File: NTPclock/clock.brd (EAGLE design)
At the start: 100 x 100 mm, 21 parts, among them IC1 MAX7219CNG

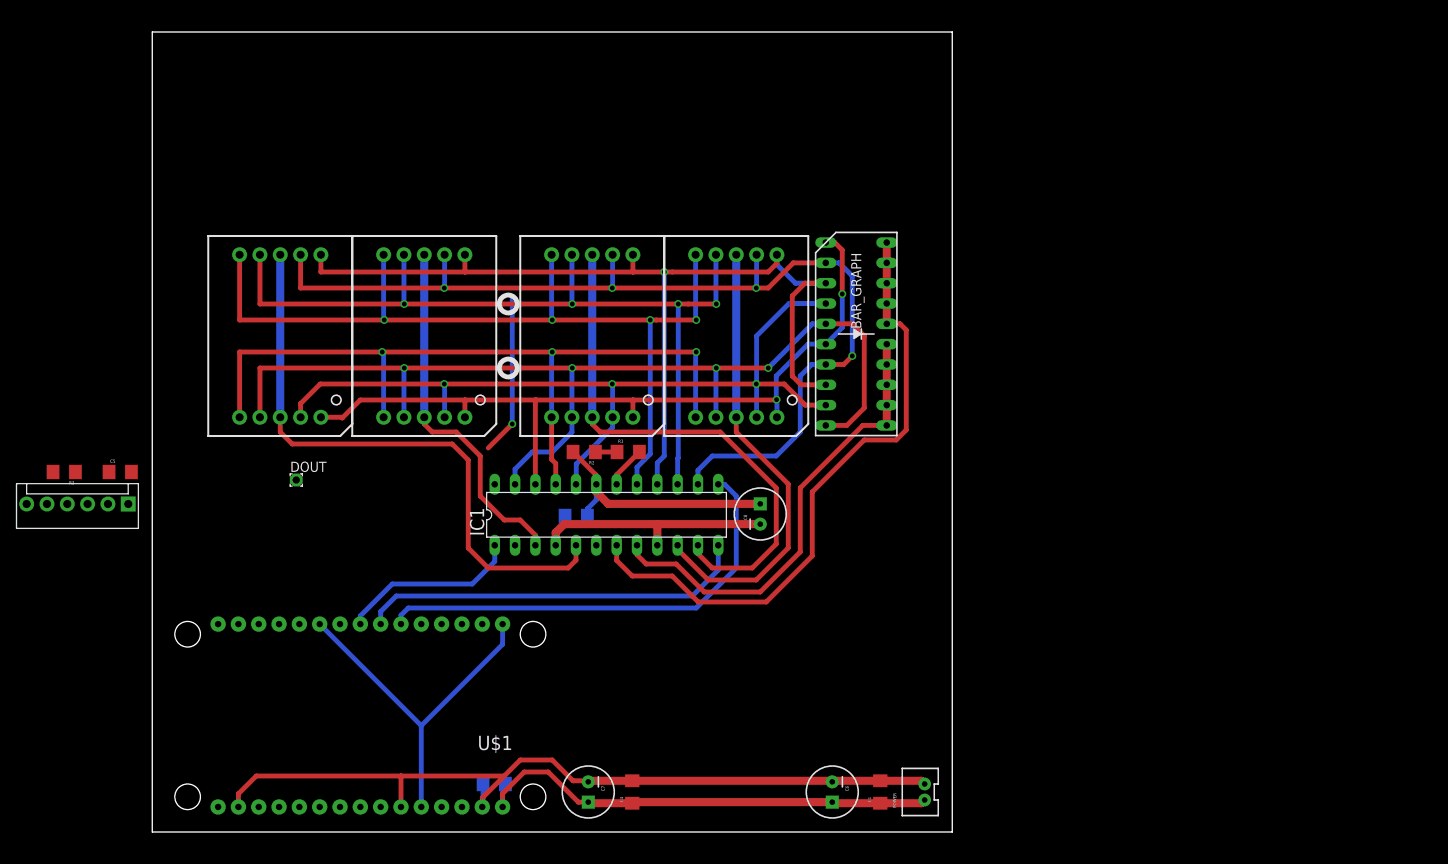
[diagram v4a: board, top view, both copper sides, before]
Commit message: Add Ground pour(s)
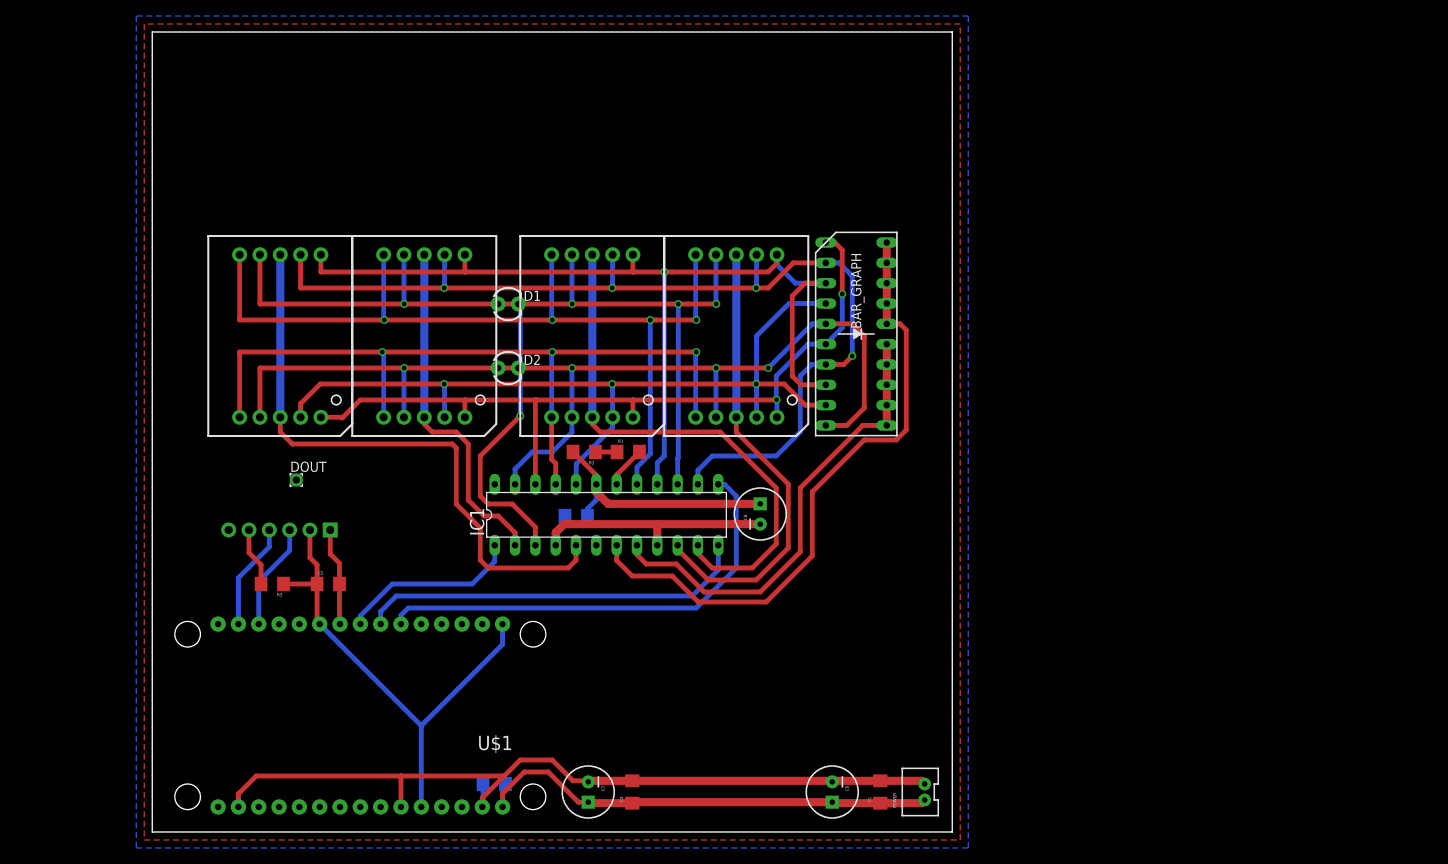
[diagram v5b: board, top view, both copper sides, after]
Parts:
- added D1, D2: (no value), SparkFun-LED:LED3MM
- moved C5 29.5 mm to (22.0, 31.0)
- moved R3 29.5 mm to (15.0, 31.0)
- moved J1 25.5 mm to (22.2, 37.8), flipped to the bottom, turned to 0 degrees
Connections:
- net DIGIT0: now also DIG_1.3, DIG_1.8
- net DIGIT4: now also D1.K, D2.K; no longer DIG_1.3, DIG_1.8
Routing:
- net DIGIT0: track 20.2 -> 43.8 mm, vias 1 -> 0
- net 3.3V: track 45.0 -> 61.5 mm
- net SDA: track 0.00 -> 13.4 mm
- net SCL: track 0.00 -> 13.4 mm
- net GND: track 136.9 -> 149.2 mm
- net DIGIT4: track 45.0 -> 37.1 mm, vias 0 -> 1
- net SQL: track 0.00 -> 7.38 mm
- added copper zone on layer 1, net GND
- added copper zone on layer 16, net GND

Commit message: added buzzer, finished routing ground plane
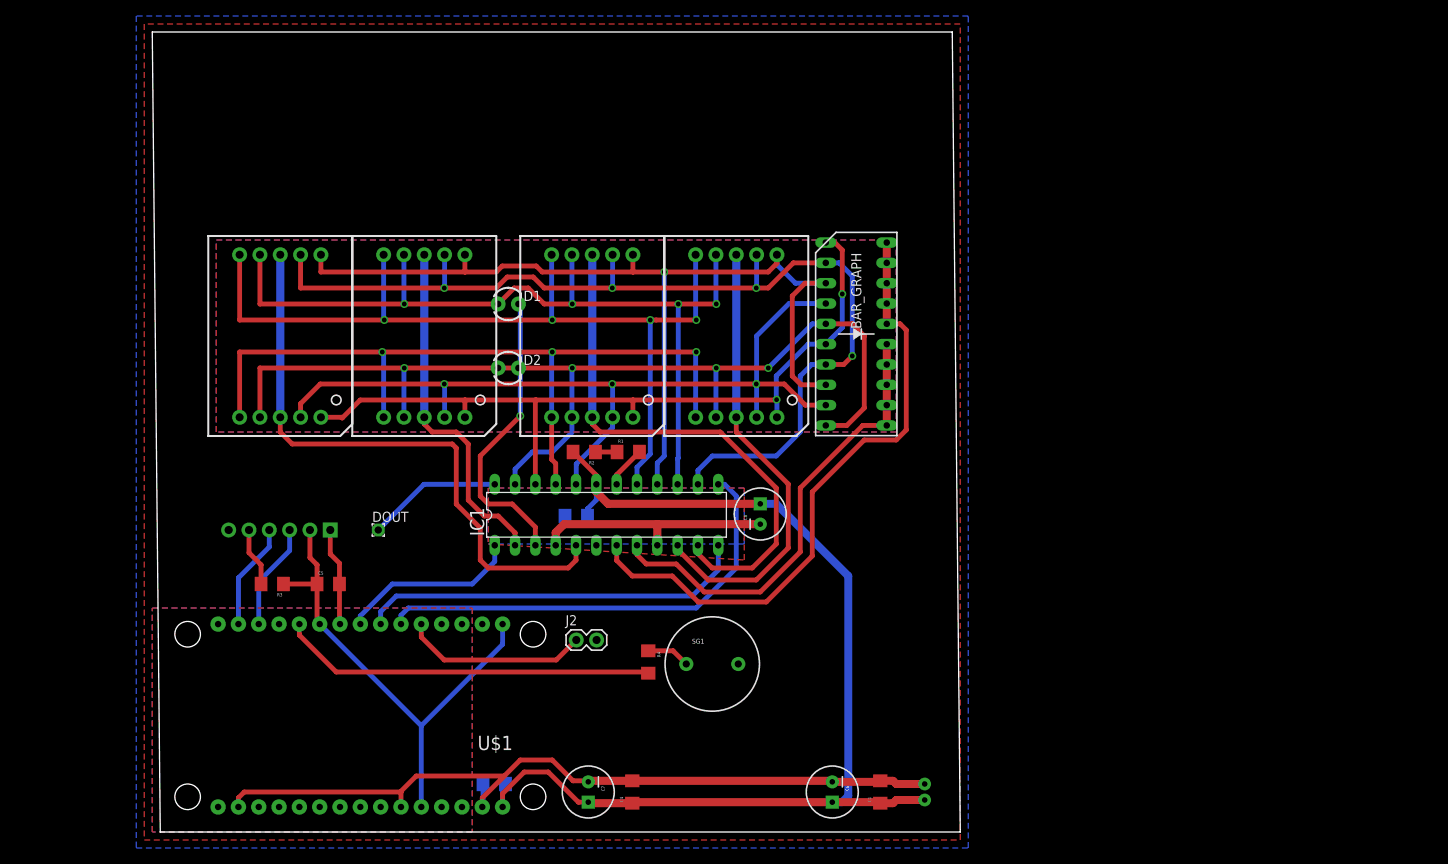
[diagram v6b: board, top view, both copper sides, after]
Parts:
- added J2: (no value), SparkFun-Connectors:1X02
- added R4: 100Ω, SparkFun-Resistors:1206
- added SG1: BUZZERPTH, SparkFun-Electromechanical:BUZZER-12MM
- moved DOUT 12.0 mm to (28.2, 37.8)
- flipped POWER to the bottom, turned to 270 degrees
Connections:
- new net D4: R4.2, U$1.D4
- new net D8: J2.1, U$1.D8
- new net N$8: R4.1, SG1.-
- net D: now also D2.A
- net F: now also D1.A
- net GND: now also J2.2, POWER.1, SG1.+; no longer POWER.2
- net VCC: now also POWER.2; no longer POWER.1
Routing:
- net D4: track 0.00 -> 47.0 mm
- net VCC: track 92.3 -> 136.9 mm
- net D8: track 0.00 -> 23.2 mm
- net DOUT: track 0.00 -> 16.9 mm
- net N$8: track 0.00 -> 5.43 mm
- net GND: track 149.2 -> 147.1 mm
- net F: track 104.4 -> 106.0 mm
- net A: track 128.8 -> 129.9 mm
- net B: track 119.7 -> 120.3 mm
- added copper zone on layer 1, net N$1
- added copper zone on layer 16, net N$2
- added copper zone on layer 1, net N$3
- added copper zone on layer 16, net N$5
- added copper zone on layer 16, net N$6
- added copper zone on layer 1, net N$7
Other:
- board size 100 x 100 mm -> 101 x 100 mm

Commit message: Correct borders
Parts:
- moved C1 1.41 mm to (90.0, 6.00)
- moved POWER 1.41 mm to (95.0, 6.00)
- moved C6 1.00 mm to (84.0, 5.00)
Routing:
- net A: track 129.9 -> 127.3 mm
- net G: track 111.2 -> 108.7 mm
- net E: track 98.6 -> 96.1 mm
- net F: track 106.0 -> 103.5 mm
- net B: track 120.3 -> 119.2 mm
- net D: track 130.7 -> 129.7 mm
- net GND: track 147.1 -> 146.3 mm
- net DP: track 101.0 -> 101.7 mm
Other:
- board size 101 x 100 mm -> 100 x 100 mm
